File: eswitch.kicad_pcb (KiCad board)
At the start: 4 copper layers, 181 x 57.5 mm, 153 parts, among them J1 Wuerth 691311400116, J2 +12V IN, J3 GND IN, J4 USB-C, J5 UART, SW1 RESET, SW2 BOOT, U1 BTS7008-1EPP, U10 ESP32-S3-WROOM-1-N8, U11 USBLC6-2SC6, U2 BTS7008-1EPP, U3 BTS7008-1EPP, U4 BTS7008-1EPP, U5 BTS7008-1EPP, U6 BTS7008-1EPP, U7 BTS7008-1EPP, U8 BTS7008-1EPP, U9 TPS54360B

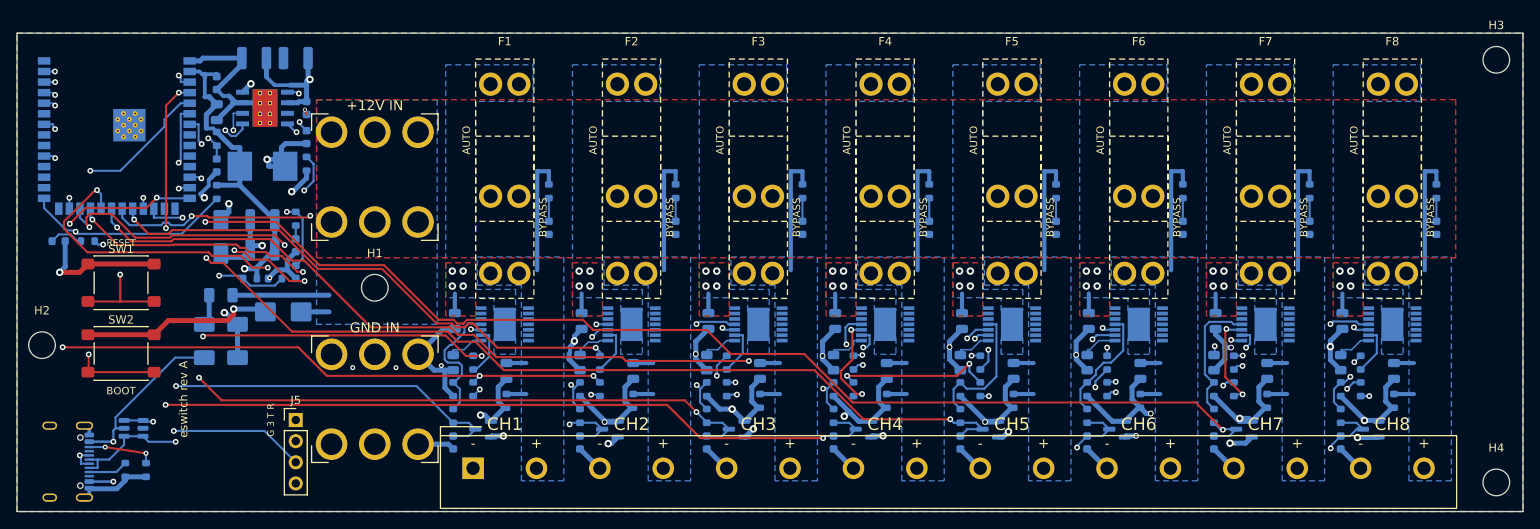
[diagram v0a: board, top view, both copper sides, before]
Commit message: Routed 1 oz board: 2x10A/5x5A/1x20A channels, DRC clean (0 copper violations, 0 unconnected)
- BTS7004/7008/7002 per rating, per-channel RSENSE, CH8 (20 A) with parallel In2 copper
- IS4 moved to IO2; decoupling/pull-ups re-placed; USB-C D+/D- tie-offs on opposite sides
- finish.py: post-route prune, fix-ups, clearance-checked grid router for hand routes
- fab/: regenerated gerbers, BOMs (DigiKey/JLCPCB/PCBWay), CPLs, 1 oz stack-up note

Co-Authored-By: Claude Fable 5.1 <noreply@anthropic.com>
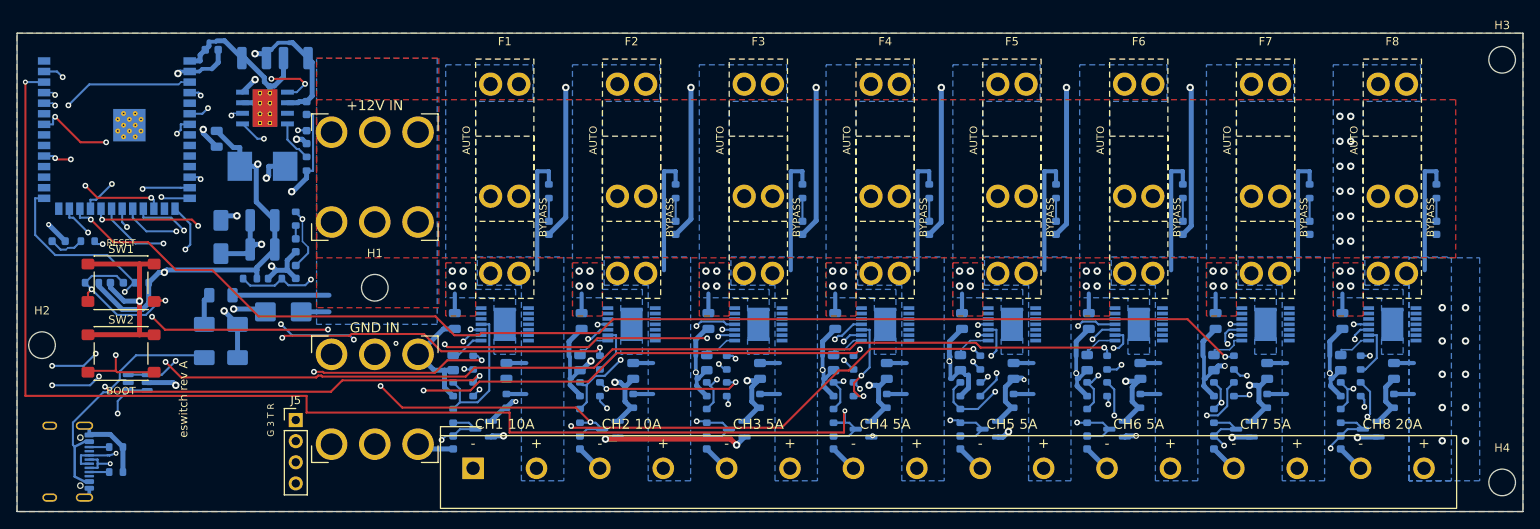
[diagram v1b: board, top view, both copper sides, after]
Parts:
- F1, F2: value ATO 15A -> ATO 10A
- F3, F4, F5, F6, F7: value ATO 15A -> ATO 5A
- F8: value ATO 15A -> ATO 20A
- R104, R204: value 1.2k 1% -> 2.2k 1%
- R304, R404, R504, R604, R704: value 1.2k 1% -> 3.3k 1%
- U1, U2: value BTS7008-1EPP -> BTS7004-1EPP
- U8: value BTS7008-1EPP -> BTS7002-1EPP
- moved R5 22.9 mm to (9.00, 30.0), turned to 180 degrees
- moved C11 18.5 mm to (12.0, 30.0), turned to 180 degrees
- moved R6 14.1 mm to (15.0, 30.0), turned to 180 degrees
- moved U11 5.52 mm to (14.5, 42.0)
- moved R8 4.53 mm to (11.9, 49.8), turned to 0 degrees
- moved C10 4.04 mm to (23.4, 2.00), turned to 180 degrees
- moved C9 3.20 mm to (24.0, 12.7)
- moved R7 1.13 mm to (11.9, 52.8), turned to 0 degrees
- moved H3 0.70 mm to (178.5, 3.20)
- moved H4 0.70 mm to (178.5, 54.0)
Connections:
- U10 pad 15: unconnected-(U10-IO3-Pad15) -> IS2
- U10 pad 18: IN1 -> IS6
- U10 pad 38: IS2 -> IS4
- U10 pad 5: IS4 -> (no net)
- U10 pad 7: IS6 -> IN1
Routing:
- net GND: track 285.6 -> 406.7 mm, vias 25 -> 29
- net IS2: track 115.5 -> 69.4 mm, vias 4 -> 3
- net IS8: track 175.8 -> 215.3 mm, vias 2 -> 5
- net +3V3: track 216.2 -> 240.6 mm, vias 9 -> 11
- net IS1: track 86.3 -> 106.0 mm
- net IN8: track 230.8 -> 211.8 mm, vias 2 -> 4
- net IS4: track 135.8 -> 154.2 mm, vias 3 -> 2
- net IN5: track 141.0 -> 123.1 mm, vias 3 -> 4
- net DEN: track 201.5 -> 219.2 mm, vias 10 -> 11
- net IS6: track 148.8 -> 132.1 mm, vias 2 -> 4
- net IN7: track 164.0 -> 148.4 mm, vias 3 -> 2
- net IS3: track 107.1 -> 93.4 mm, vias 4 -> 2
- net EN: track 47.0 -> 60.0 mm
- net VIN: track 55.2 -> 66.1 mm
- net IO0: track 50.4 -> 39.6 mm
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- added copper zone on In2.Cu, net LOAD8
- added copper zone on In2.Cu, net VS8
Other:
- board text added: "CH1 10A"
- board text added: "CH2 10A"
- board text added: "CH3 5A"
- board text added: "CH4 5A"
- board text added: "CH5 5A"
- board text added: "CH6 5A"
- board text added: "CH7 5A"
- board text added: "CH8 20A"
- board text removed: "CH1"
- board text removed: "CH2"
- board text removed: "CH3"
- board text removed: "CH4"
- board text removed: "CH5"
- board text removed: "CH6"
- board text removed: "CH7"
- board text removed: "CH8"
